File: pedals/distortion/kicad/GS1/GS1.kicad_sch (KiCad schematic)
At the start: 0 parts

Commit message: Add bias voltage section to GS1 schematic; ignore KiCad local history
Co-Authored-By: Claude Opus 5.5 <noreply@anthropic.com>
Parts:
- added C6: 10u, symbol Device:C_Polarized
- added C7: 100u, symbol Device:C_Polarized
- added R7: 1M, Package_QFP:PQFP-160_28x28mm_P0.65mm, symbol Device:R
- added R8: 1M, symbol Device:R
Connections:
- new net +9V: C7.1, R7.1
- new net GND: C6.2, C7.2, R8.2
- new net VB: C6.1, R7.2, R8.1

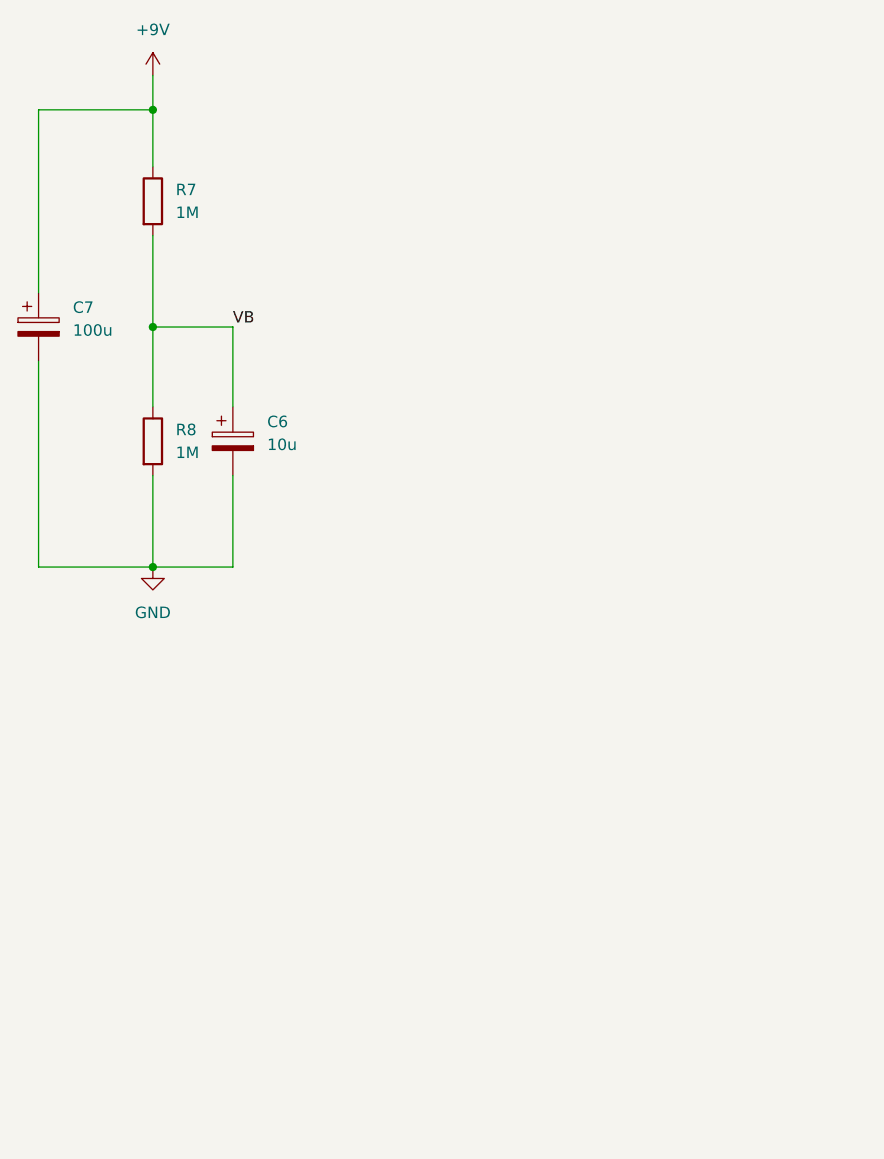
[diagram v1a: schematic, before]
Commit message: Add input section to GS1 schematic
Co-Authored-By: Claude Opus 5.5 <noreply@anthropic.com>
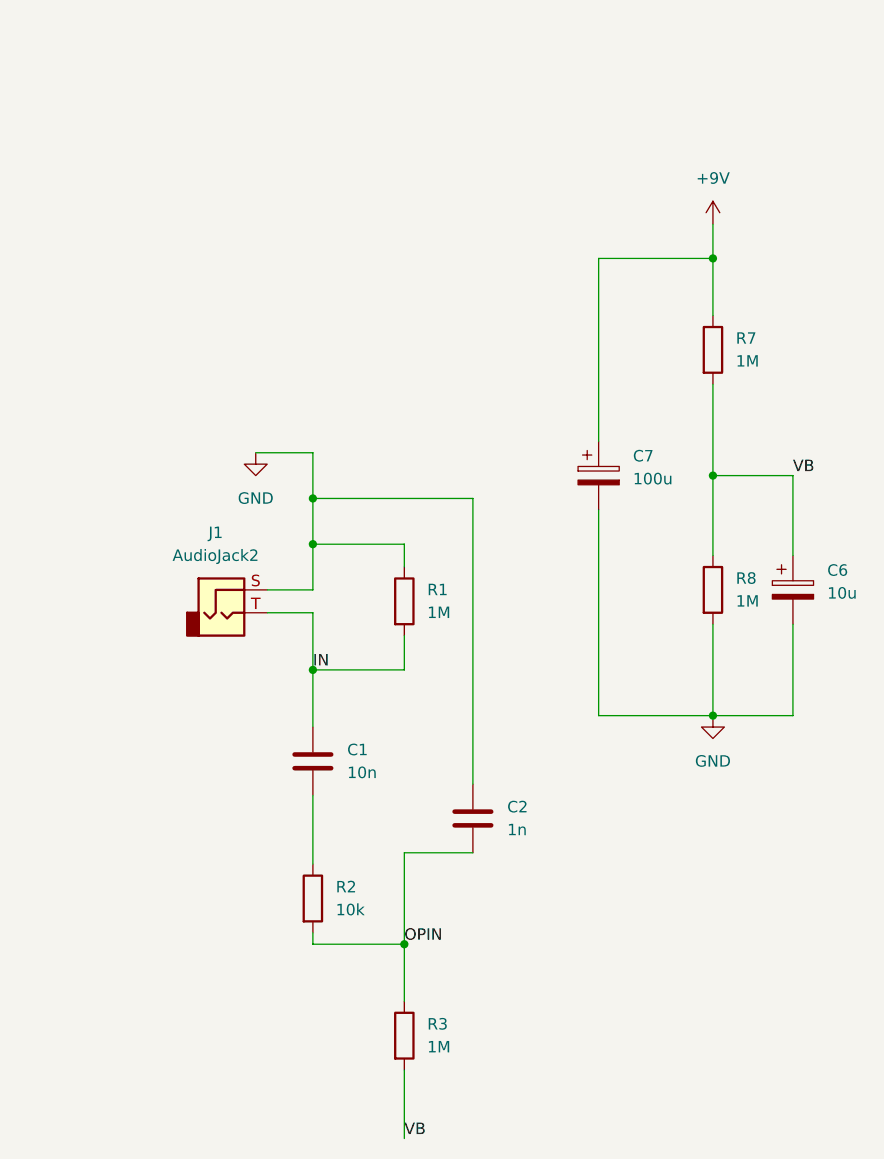
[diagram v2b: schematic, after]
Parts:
- added C1: 10n, Package_QFP:PQFP-160_28x28mm_P0.65mm, symbol Device:C
- added C2: 1n, Package_QFP:PQFP-160_28x28mm_P0.65mm, symbol Device:C
- added J1: AudioJack2, Connector_Audio:Jack_XLR_Neutrik_NC3FAAH_Horizontal, symbol Connector_Audio:AudioJack2
- added R1, R3: 1M, Package_QFP:PQFP-160_28x28mm_P0.65mm, symbol Device:R
- added R2: 10k, Package_QFP:PQFP-160_28x28mm_P0.65mm, symbol Device:R
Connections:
- net GND: now also C2.1, J1.S, R1.1
- net VB: now also R3.2
- new net: C1.2, R2.1
- new net IN: C1.1, J1.T, R1.2
- new net OPIN: C2.2, R2.2, R3.1
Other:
- moved on the sheet: C6, C7, R7, R8

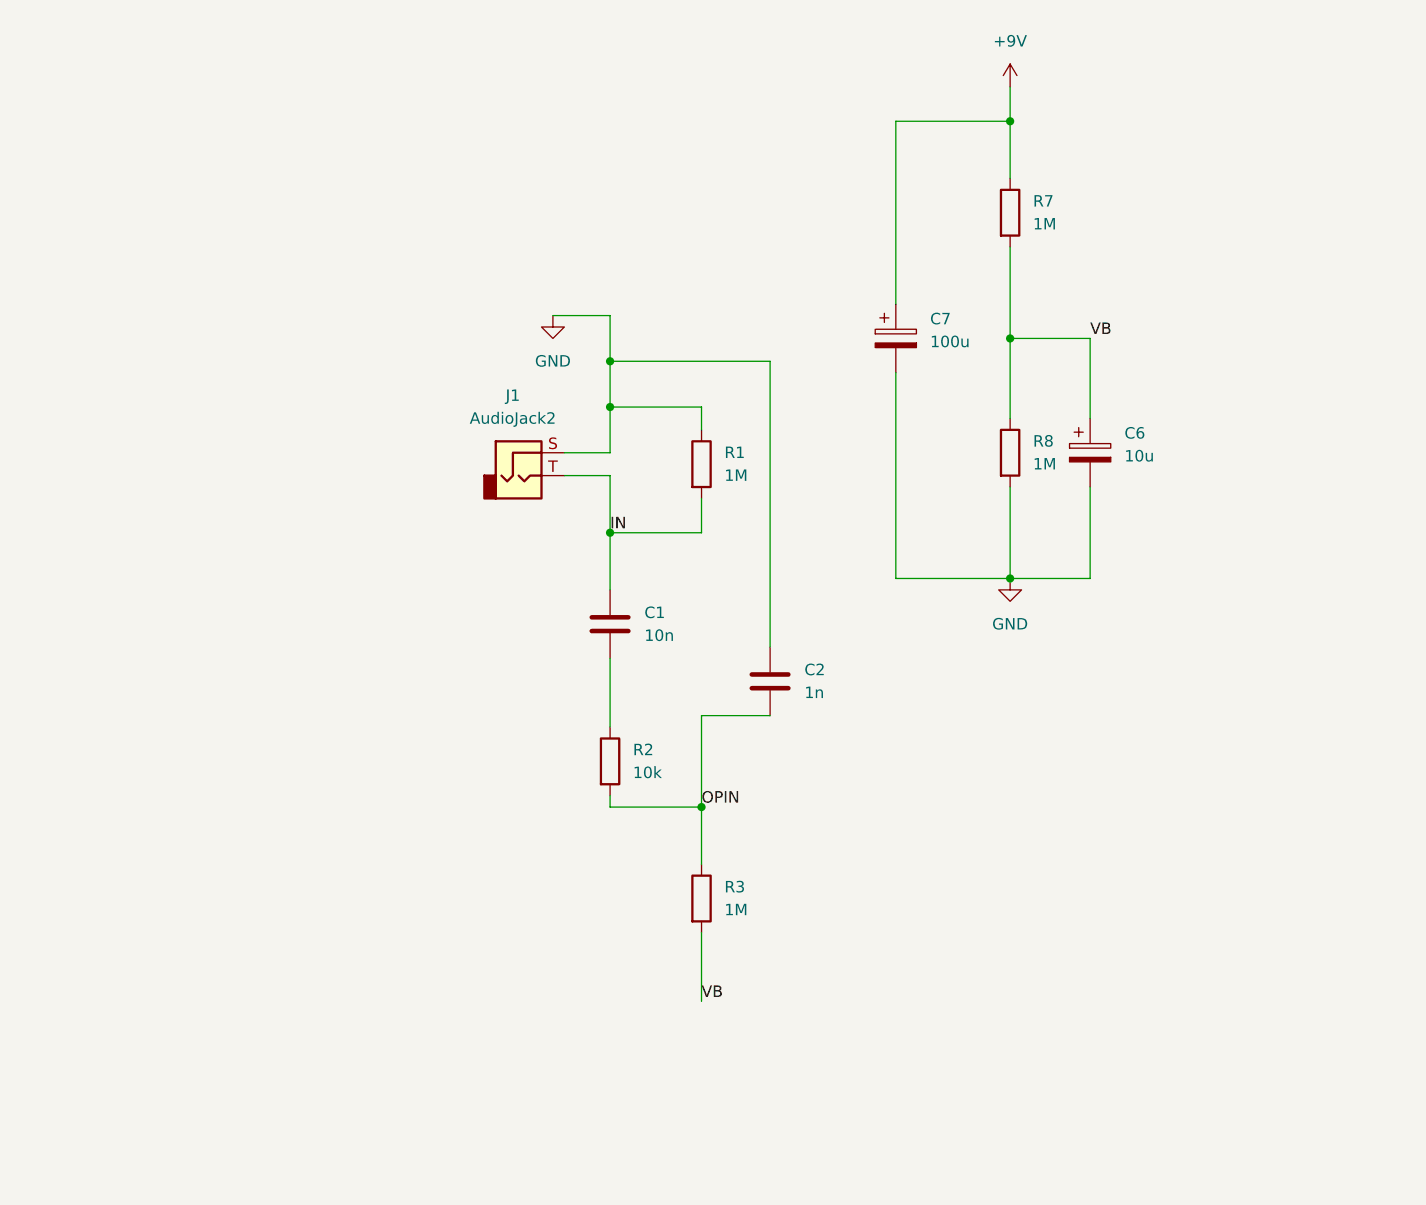
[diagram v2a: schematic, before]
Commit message: Add op-amp gain stage to GS1 schematic
Co-Authored-By: Claude Opus 5.5 <noreply@anthropic.com>
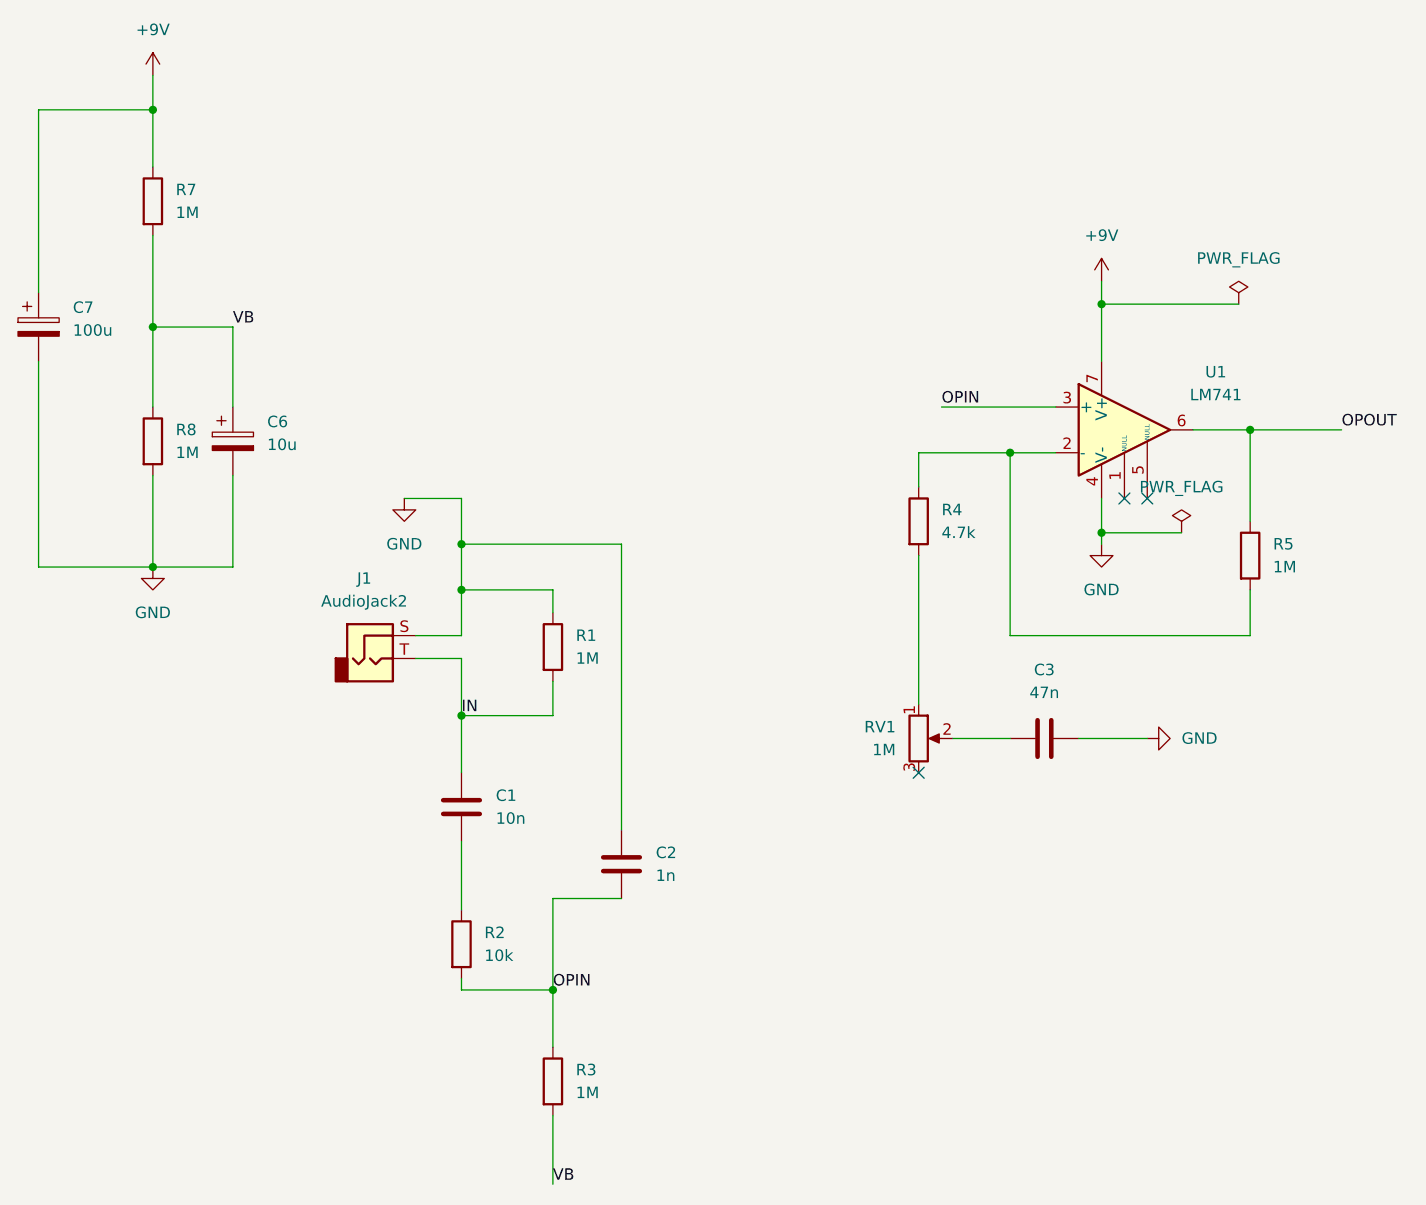
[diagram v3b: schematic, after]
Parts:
- added C3: 47n, Package_QFP:PQFP-160_28x28mm_P0.65mm, symbol Device:C
- added R4: 4.7k, symbol Device:R
- added R5: 1M, Package_QFP:PQFP-160_28x28mm_P0.65mm, symbol Device:R
- added RV1: 1M, symbol Device:R_Potentiometer
- added U1: LM741, Package_TO_SOT_SMD:SOT-23-6, symbol Amplifier_Operational:LM741
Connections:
- net +9V: now also U1.7 (V+)
- net GND: now also C3.2, U1.4 (V-)
- net OPIN: now also U1.3 (+)
- new net: R4.1, R5.2, U1.2 (-)
- new net: R4.2, RV1.1
- new net: C3.1, RV1.2
- new net OPOUT: R5.1, U1.6
- no-connect marks 0 -> 3
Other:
- moved on the sheet: C1, C2, C6, C7, J1, R1, R2, R3, R7, R8

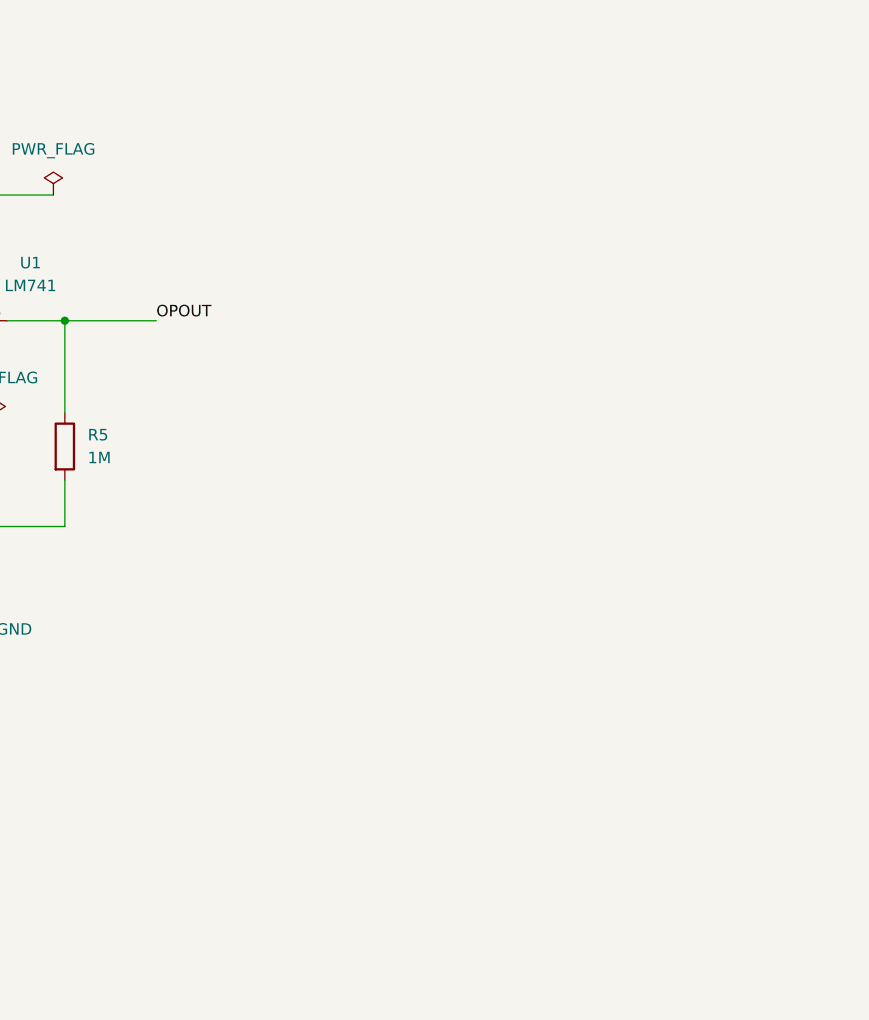
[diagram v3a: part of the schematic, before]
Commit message: Complete GS1 schematic with output and clipping section
Co-Authored-By: Claude Opus 5.5 <noreply@anthropic.com>
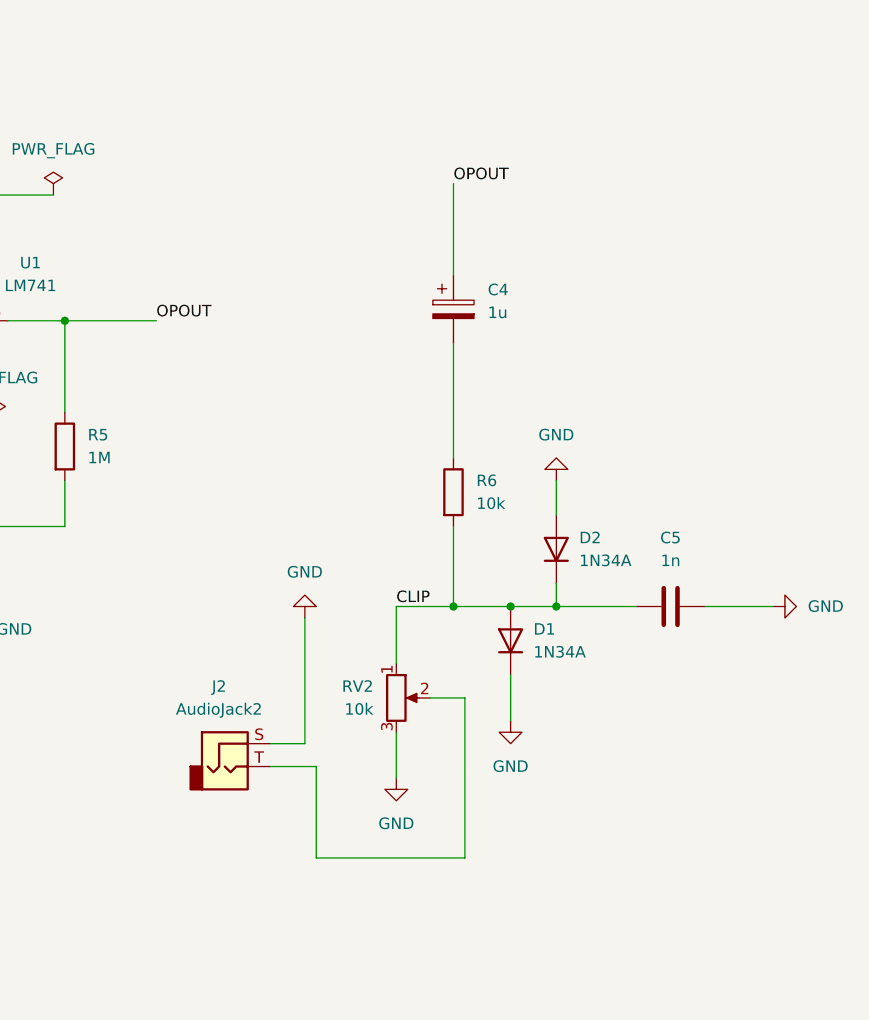
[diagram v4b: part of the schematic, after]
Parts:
- added C4: 1u, symbol Device:C_Polarized
- added C5: 1n, Package_QFP:PQFP-160_28x28mm_P0.65mm, symbol Device:C
- added D1, D2: 1N34A, Package_QFP:PQFP-160_28x28mm_P0.65mm, symbol Device:D
- added J2: AudioJack2, Connector_Audio:Jack_XLR_Neutrik_NC3FAAH_Horizontal, symbol Connector_Audio:AudioJack2
- added R6: 10k, symbol Device:R
- added RV2: 10k, Package_QFP:PQFP-160_28x28mm_P0.65mm, symbol Device:R_Potentiometer
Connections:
- net GND: now also C5.1, D1.1 (K), D2.2 (A), J2.S, RV2.3
- net OPOUT: now also C4.1
- new net: J2.T, RV2.2
- new net: C4.2, R6.1
- new net CLIP: C5.2, D1.2 (A), D2.1 (K), R6.2, RV2.1
